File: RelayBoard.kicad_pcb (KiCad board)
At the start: 4 copper layers, 211.1 x 95.2 mm, 118 parts, among them J1 OSTTC020162, J10 24VAC In, J11 OSTTC020162, J12 OSTTC020162, J13 OSTTC020162, J14 OSTTC020162, J15 OSTTC020162, J16 OSTTC020162, J17 OSTTC020162, J18 OSTTC020162, J19 Raspberry_Pi_2_3, J2 OSTTC020162, J20 OSTTC020162, J22 Conn_01x04, J3 OSTTC020162, J4 OSTTC020162, J5 OSTTC020162, J6 OSTTC020162, J7 OSTTC020162, J8 OSTTC020162, J9 PJ-202A, K1 AQY212GHAX, K11 AQY212GHAX, K12 AQY212GHAX, K13 AQY212GHAX, K14 AQY212GHAX, K15 AQY212GHAX, K16 AQY212GHAX, K17 AQY212GHAX, K18 AQY212GHAX, K2 AQY212GHAX, K3 AQY212GHAX, K4 AQY212GHAX, K5 AQY212GHAX, K6 AQY212GHAX, K7 AQY212GHAX, K8 AQY212GHAX, U1 AP1117-50

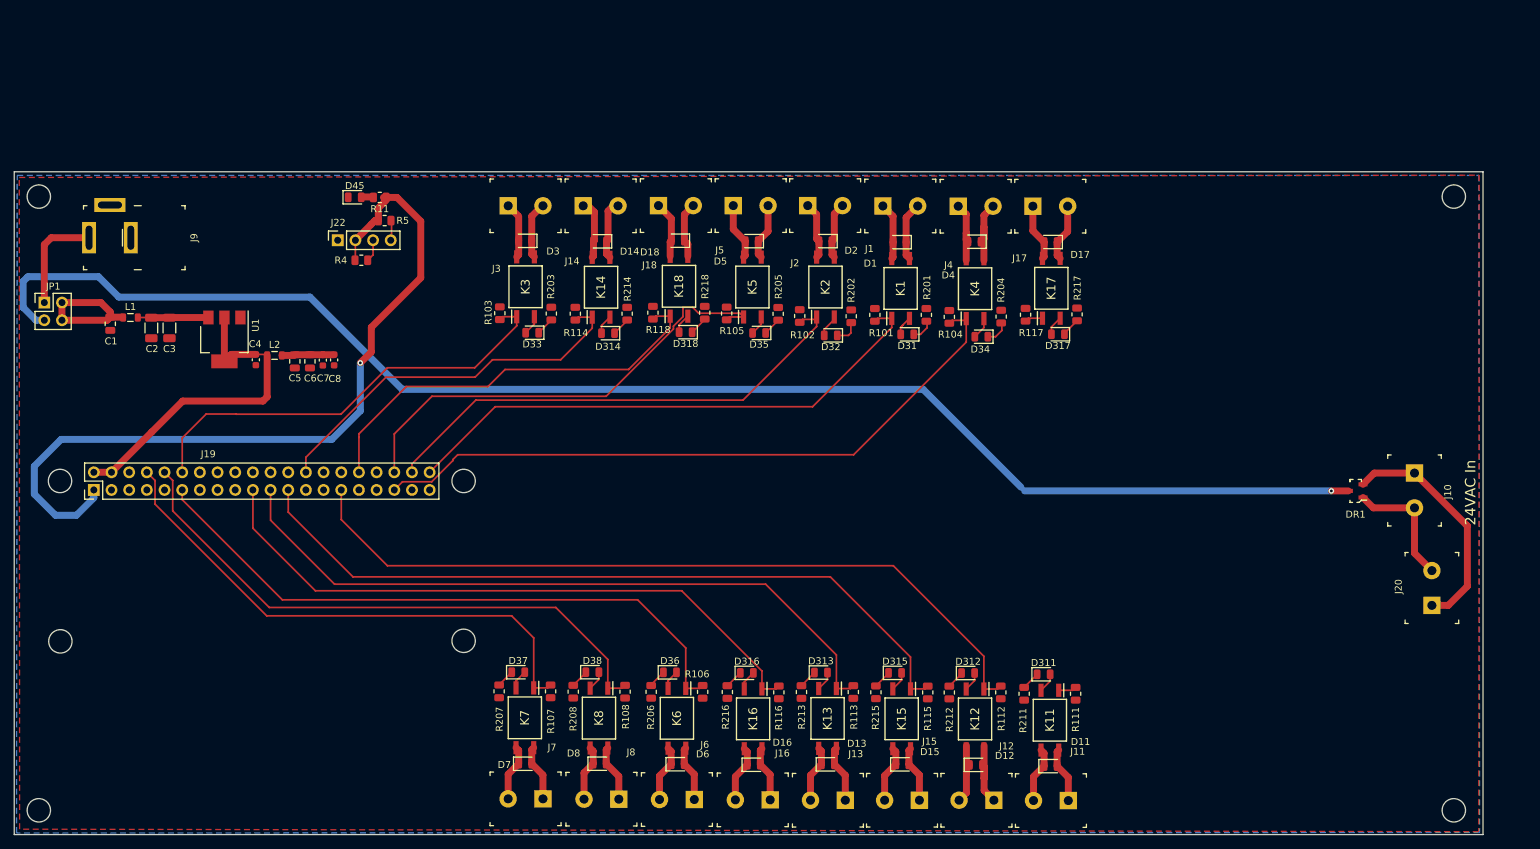
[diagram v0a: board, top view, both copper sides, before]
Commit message: fix drc errors, change bottom zone to GND
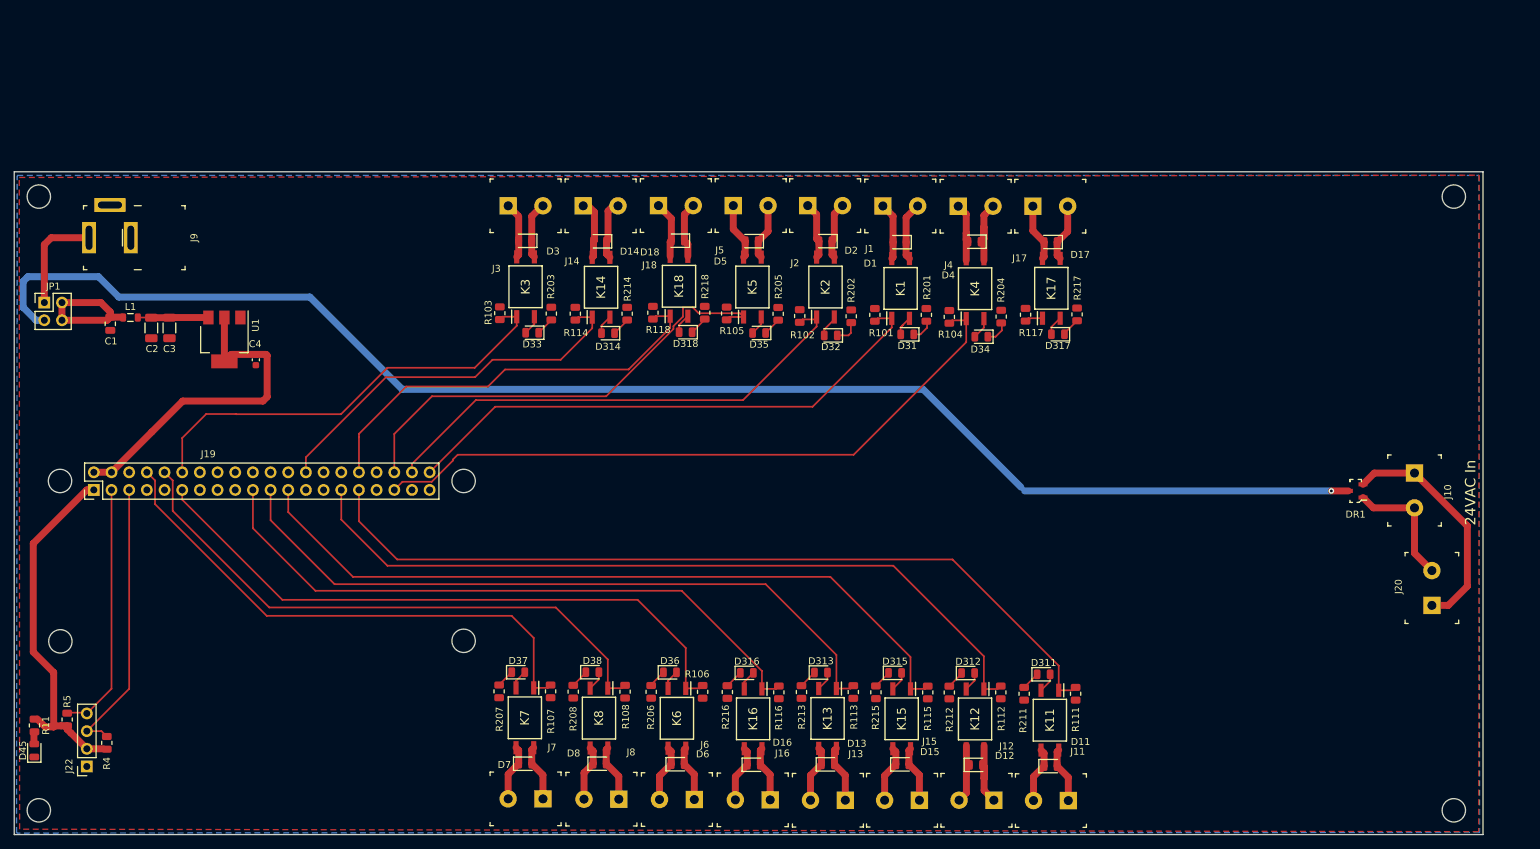
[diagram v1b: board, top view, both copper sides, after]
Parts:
- removed C5: 100n, Capacitor_SMD:C_0805_2012Metric
- removed C6: 10n, Capacitor_SMD:C_0805_2012Metric
- removed C7: 1n, Capacitor_SMD:C_0603_1608Metric
- removed C8: 100n, Capacitor_SMD:C_0603_1608Metric
- removed L2: 10uH, Inductor_SMD:L_0805_2012Metric
- moved D45 91.9 mm to (20.1, 148.9), turned to 90 degrees
- moved R11 90.7 mm to (20.2, 145.4), turned to -90 degrees
- moved R5 85.0 mm to (24.9, 144.5), turned to 90 degrees
- moved J22 83.8 mm to (27.7, 151.2), turned to 180 degrees
- moved R4 78.4 mm to (30.6, 147.9), turned to 90 degrees
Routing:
- net Net-(J19-Pad31): track 2.60 -> 119.8 mm
- net +3V3: track 114.4 -> 51.6 mm, vias 1 -> 0
- net I2C_SDA: track 64.8 -> 35.9 mm
- net I2C_SCL: track 58.8 -> 40.4 mm
- net Net-(C5-Pad1): track 7.59 -> 0.00 mm
- added copper zone on B.Cu, net GND
- removed copper zone on In1.Cu, net GND
- removed copper zone on B.Cu, net Net-(C5-Pad1)
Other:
- copper layers 4 -> 2

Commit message: resize board
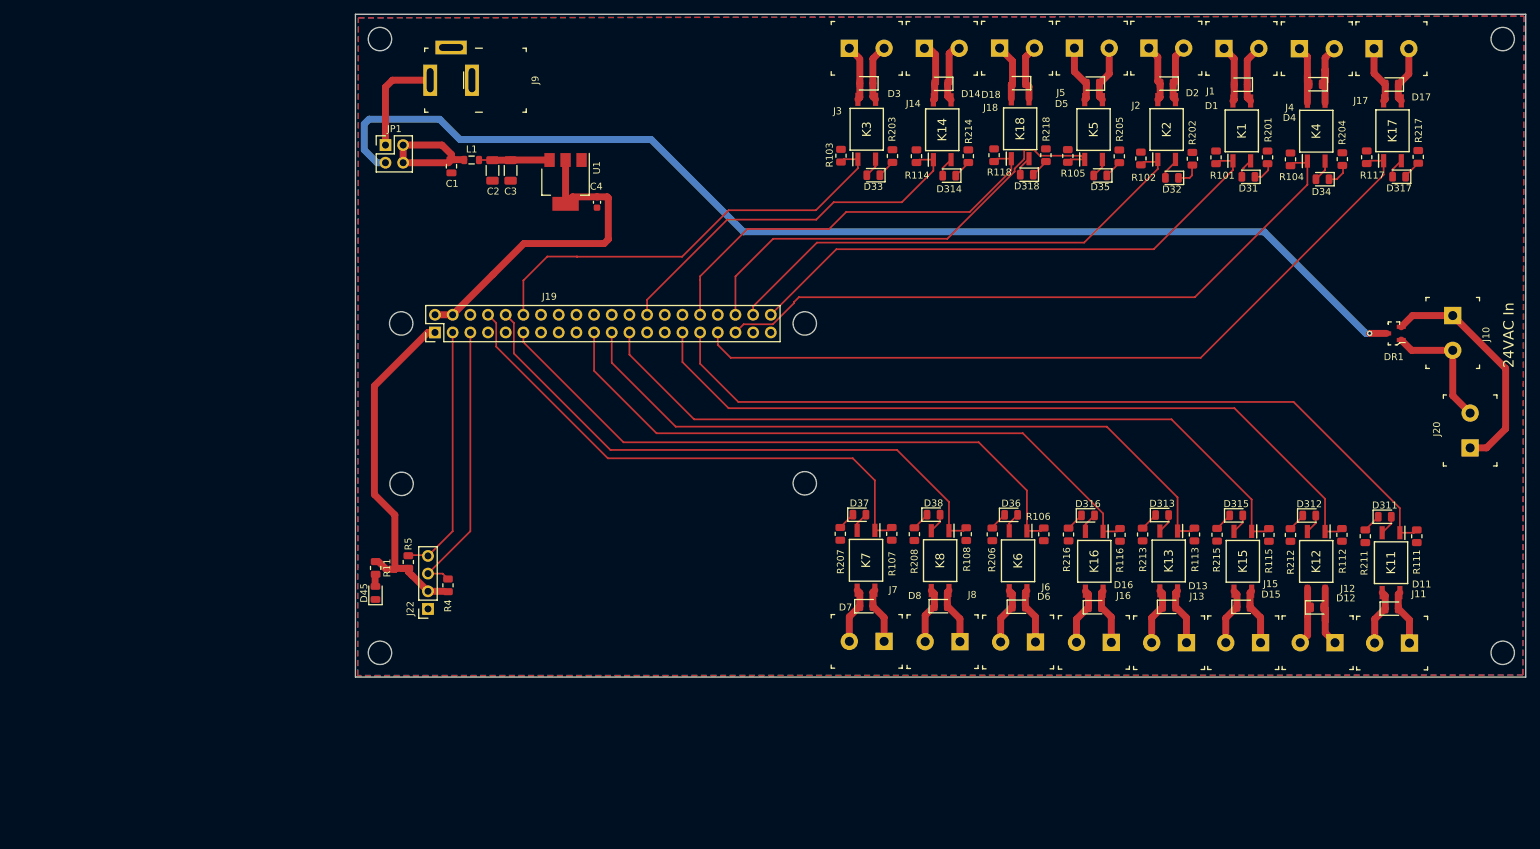
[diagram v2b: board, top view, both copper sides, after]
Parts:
- moved D11 54.0 mm to (215.2, 128.6)
- moved D13 54.0 mm to (183.2, 128.3)
- moved D311 54.0 mm to (214.2, 115.4)
- moved D313 54.0 mm to (182.2, 115.1)
- moved D318 54.0 mm to (162.8, 66.2)
- moved D36 54.0 mm to (160.5, 115.1)
- moved J13 54.0 mm to (185.7, 133.5)
- moved K6 54.0 mm to (161.5, 121.7)
- moved R101 54.0 mm to (190.0, 63.7)
- moved R112 54.0 mm to (208.1, 118.0)
- moved R117 54.0 mm to (211.6, 63.7)
- moved R218 54.0 mm to (165.5, 63.4)
- moved C2 54.0 mm to (86.0, 65.6)
- moved C3 54.0 mm to (88.6, 65.6)
- moved C4 54.0 mm to (101.0, 70.2)
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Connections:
- J19 pad 17: +3V3 -> unconnected-(J19-Pad17)
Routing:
- net Net-(J19-Pad33): track 2.60 -> 113.8 mm
- net 16VDC Unregulated In from AC: track 210.3 -> 167.5 mm
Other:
- board size 211.1 x 95.2 mm -> 168.2 x 95.2 mm
